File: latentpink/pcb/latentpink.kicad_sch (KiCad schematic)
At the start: 28 parts, among them M10 WEEE, M3 SCREWHOLE, M4 SCREWHOLE, M5 SCREWHOLE, M6 SCREWHOLE, M7 LONGTHING, M8 OSHW, M9 POLARITY, U36 AT30TS74_UDFN, U37 AT30TS74_UDFN, U38 AT30TS74_UDFN, U39 AT30TS74_UDFN

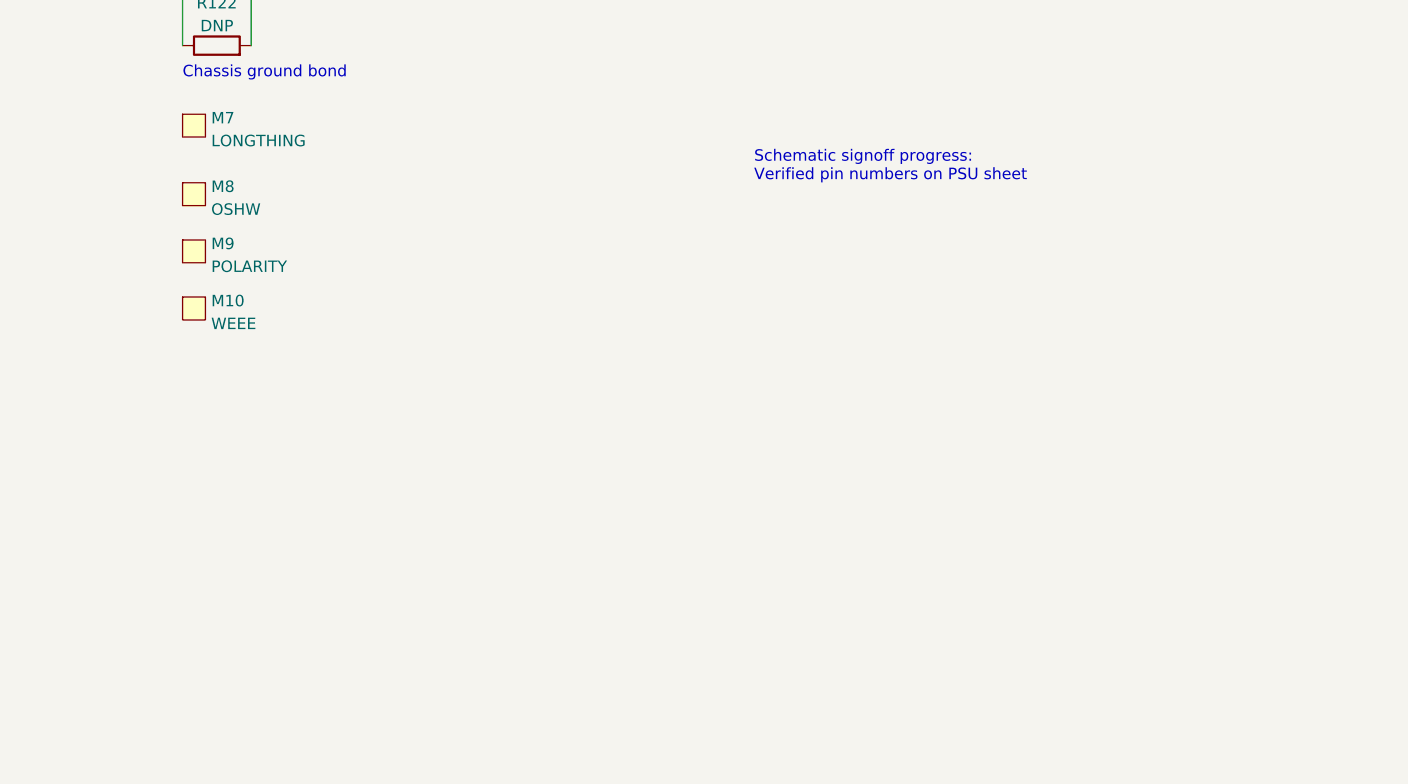
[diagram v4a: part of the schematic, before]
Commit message: Continued work on signoff review, added some more test points and SFP+ activity LEDs
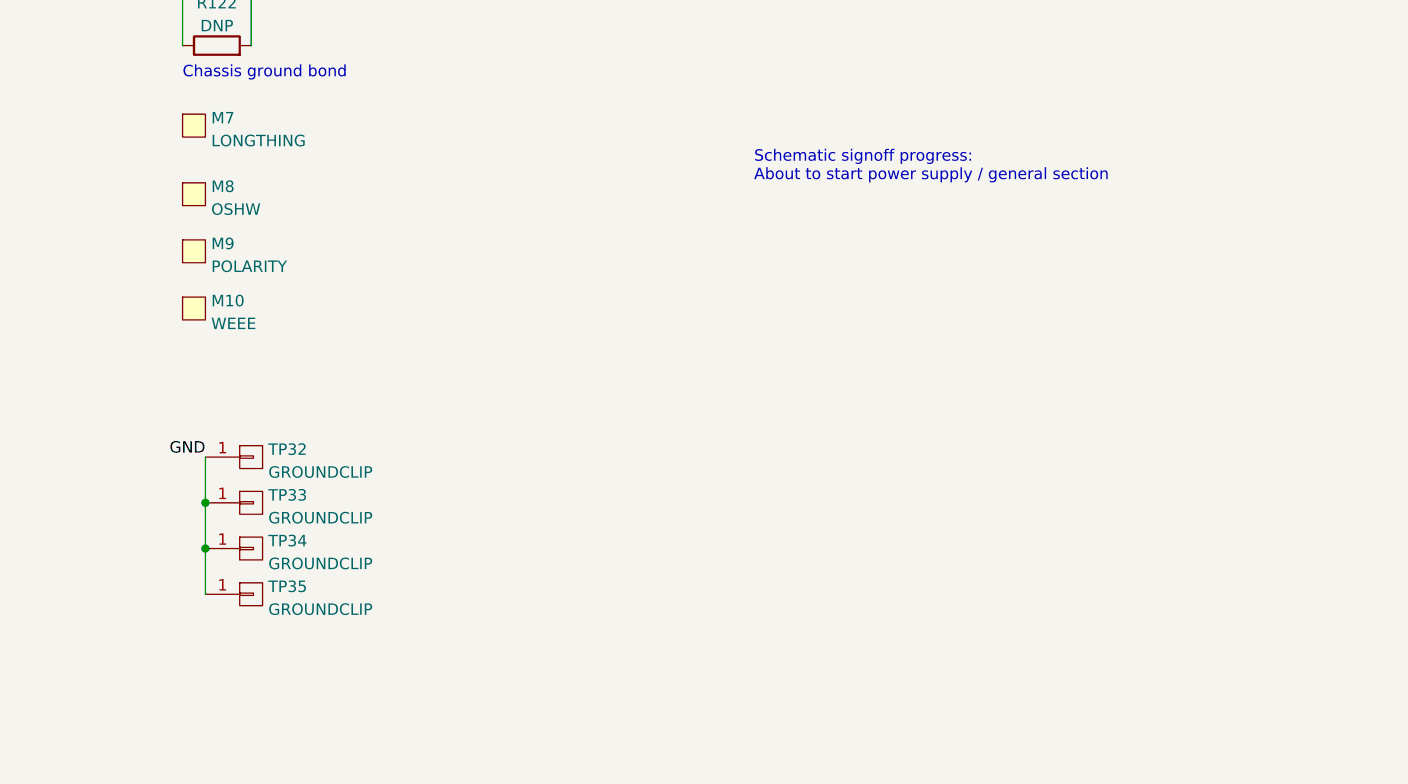
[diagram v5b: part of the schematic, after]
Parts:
- added TP32, TP33, TP34, TP35: GROUNDCLIP, azonenberg_pcb:TESTPOINT_SMT_KEYSTONE_5016, symbol conn:CONN_01X01
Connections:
- net GND: now also TP32.1 (P1), TP33.1 (P1), TP34.1 (P1), TP35.1 (P1)
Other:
- note added: "Schematic signoff progress: About to start power supply / general section"
- note removed: "Schematic signoff progress: Verified pin numbers on PSU sheet"
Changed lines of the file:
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@@
   (title_block
     (title "LATENTPINK - Top Level")
-    (date "2023-05-20")
+    (date "2023-05-21")
     (rev "0.1")
     (company "Antikernel Labs")
     (comment 1 "Andrew D. Zonenberg")
   )
+  (junction (at 72.39 173.99) (diameter 0) (color 0 0 0 0)
+  )
+  (junction (at 72.39 168.91) (diameter 0) (color 0 0 0 0)
+  )
   (no_connect (at 316.23 93.98))
   (no_connect (at 316.23 33.02))
@@
     (stroke (width 0) (type default) (color 0 0 0 0))
   )
+  (wire (pts (xy 72.39 173.99) (xy 72.39 179.07))
+    (stroke (width 0) (type default) (color 0 0 0 0))
+  )
   (wire (pts (xy 30.48 190.5) (xy 34.29 190.5))
     (stroke (width 0) (type default) (color 0 0 0 0))
@@
     (stroke (width 0) (type default) (color 0 0 0 0))
   )
+  (wire (pts (xy 72.39 168.91) (xy 72.39 173.99))
+    (stroke (width 0) (type default) (color 0 0 0 0))
+  )
   (wire (pts (xy 30.48 120.65) (xy 34.29 120.65))
     (stroke (width 0) (type default) (color 0 0 0 0))
@@
     (stroke (width 0) (type default) (color 0 0 0 0))
   )
-  (text "Schematic signoff progress:\nVerified pin numbers on PSU sheet"
+  (wire (pts (xy 72.39 163.83) (xy 72.39 168.91))
+    (stroke (width 0) (type default) (color 0 0 0 0))
+  )
+  (text "Schematic signoff progress:\nAbout to start power supply / general section"
     (at 133.35 133.35 0)
     (effects (font (size 1.27 1.27)) (justify left bottom))
@@
     (effects (font (size 1.27 1.27)) (justify left bottom))
   )
+  (label "GND" (at 72.39 163.83 180)
+    (effects (font (size 1.27 1.27)) (justify right bottom))
+  )
   (label "TEMP_I2C_SDA" (at 295.91 30.48 180)
     (effects (font (size 1.27 1.27)) (justify right bottom))
@@
     )
   )
+  (symbol (lib_id "conn:CONN_01X01") (at 77.47 168.91 0) (unit 1)
+    (in_bom yes) (on_board yes) (fields_autoplaced)
+    (property "Reference" "TP33" (id 0) (at 79.375 168.0753 0)
+      (effects (font (size 1.27 1.27)) (justify left))
+    )
+    (property "Value" "GROUNDCLIP" (id 1) (at 79.375 170.6122 0)
+      (effects (font (size 1.27 1.27)) (justify left))
+    )
+    (property "Footprint" "azonenberg_pcb:TESTPOINT_SMT_KEYSTONE_5016" (id 2) (at 77.47 168.91 0)
+      (effects (font (size 1.27 1.27)) hide)
+    )
+    (property "Datasheet" "" (id 3) (at 77.47 168.91 0)
+      (effects (font (size 1.27 1.27)) hide)
+    )
+    (pin "1")
+  )
   (symbol (lib_id "device:C") (at 337.82 44.45 0) (unit 1)
     (in_bom yes) (on_board yes) (fields_autoplaced)
@@
     (pin "2")
   )
+  (symbol (lib_id "conn:CONN_01X01") (at 77.47 173.99 0) (unit 1)
+    (in_bom yes) (on_board yes) (fields_autoplaced)
+    (property "Reference" "TP34" (id 0) (at 79.375 173.1553 0)
+      (effects (font (size 1.27 1.27)) (justify left))
+    )
+    (property "Value" "GROUNDCLIP" (id 1) (at 79.375 175.6922 0)
+      (effects (font (size 1.27 1.27)) (justify left))
+    )
+    (property "Footprint" "azonenberg_pcb:TESTPOINT_SMT_KEYSTONE_5016" (id 2) (at 77.47 173.99 0)
+      (effects (font (size 1.27 1.27)) hide)
+    )
+    (property "Datasheet" "" (id 3) (at 77.47 173.99 0)
+      (effects (font (size 1.27 1.27)) hide)
+    )
+    (pin "1")
+  )
+  (symbol (lib_id "conn:CONN_01X01") (at 77.47 163.83 0) (unit 1)
+    (in_bom yes) (on_board yes) (fields_autoplaced)
+    (property "Reference" "TP32" (id 0) (at 79.375 162.9953 0)
+      (effects (font (size 1.27 1.27)) (justify left))
+    )
+    (property "Value" "GROUNDCLIP" (id 1) (at 79.375 165.5322 0)
+      (effects (font (size 1.27 1.27)) (justify left))
+    )
+    (property "Footprint" "azonenberg_pcb:TESTPOINT_SMT_KEYSTONE_5016" (id 2) (at 77.47 163.83 0)
+      (effects (font (size 1.27 1.27)) hide)
+    )
+    (property "Datasheet" "" (id 3) (at 77.47 163.83 0)
+      (effects (font (size 1.27 1.27)) hide)
+    )
+    (pin "1")
+  )
   (symbol (lib_id "device:Ferrite_Bead_Small") (at 72.39 109.22 90) (unit 1)
     (in_bom yes) (on_board yes) (fields_autoplaced)
@@
     (pin "2")
   )
+  (symbol (lib_id "conn:CONN_01X01") (at 77.47 179.07 0) (unit 1)
+    (in_bom yes) (on_board yes) (fields_autoplaced)
+    (property "Reference" "TP35" (id 0) (at 79.375 178.2353 0)
+      (effects (font (size 1.27 1.27)) (justify left))
+    )
+    (property "Value" "GROUNDCLIP" (id 1) (at 79.375 180.7722 0)
+      (effects (font (size 1.27 1.27)) (justify left))
+    )
+    (property "Footprint" "azonenberg_pcb:TESTPOINT_SMT_KEYSTONE_5016" (id 2) (at 77.47 179.07 0)
+      (effects (font (size 1.27 1.27)) hide)
+    )
+    (property "Datasheet" "" (id 3) (at 77.47 179.07 0)
+      (effects (font (size 1.27 1.27)) hide)
+    )
+    (pin "1")
+  )
   (symbol (lib_id "conn:CONN_COAXIAL") (at 34.29 185.42 0) (unit 1)
     (in_bom yes) (on_board yes) (fields_autoplaced)
@@
       (reference "D15") (unit 1) (value "GREEN") (footprint "azonenberg_pcb:EIA_0603_LED")
     )
+    (path "/035a8a96-1dae-486c-a84e-a11c0c87b4ac/9e161449-e137-4951-be09-6af8631656a8"
+      (reference "D16") (unit 1) (value "GREEN") (footprint "azonenberg_pcb:EIA_0603_LED")
+    )
+    (path "/035a8a96-1dae-486c-a84e-a11c0c87b4ac/40a9ff30-f90c-4171-be6b-c57887c62da3"
+      (reference "D17") (unit 1) (value "GREEN") (footprint "azonenberg_pcb:EIA_0603_LED")
+    )
     (path "/70fb61fd-2f76-4850-9d6b-7e1d9a86570a/d67410e9-b9d7-4681-a748-c3dfbad70b7a"
       (reference "F1") (unit 1) (value "ERB-RD4R00X") (footprint "azonenberg_pcb:EIA_0402_CAP_NOSILK")
@@
       (reference "R163") (unit 1) (value "470") (footprint "azonenberg_pcb:EIA_0402_RES_NOSILK")
     )
+    (path "/035a8a96-1dae-486c-a84e-a11c0c87b4ac/abe3af9d-8d07-4694-83b0-02bd2d2b72e0"
+      (reference "R164") (unit 1) (value "470") (footprint "azonenberg_pcb:EIA_0402_RES_NOSILK")
+    )
+    (path "/035a8a96-1dae-486c-a84e-a11c0c87b4ac/1c30b4cc-1c78-4d4a-b045-9913b60da471"
+      (reference "R165") (unit 1) (value "470") (footprint "azonenberg_pcb:EIA_0402_RES_NOSILK")
+    )
+    (path "/70fb61fd-2f76-4850-9d6b-7e1d9a86570a/257db866-fb51-4837-970d-eba7d6636664"
+      (reference "R166") (unit 1) (value "0") (footprint "azonenberg_pcb:EIA_0402_RES_NOSILK")
+    )
     (path "/6c4b0638-d970-4292-bc58-db2e1b793524/d5990d76-6ad3-4bfd-a9be-5da547fd1224/4d701df3-1531-4e26-be52-80b3fa172f57"
       (reference "RN1") (unit 1) (value "YC124-FR-0749R9L") (footprint "azonenberg_pcb:YAGEO_YC124-FR")
@@
       (reference "TP27") (unit 1) (value "U.FL") (footprint "azonenberg_pcb:CONN_U.FL_TE_1909763-1")
     )
+    (path "/035a8a96-1dae-486c-a84e-a11c0c87b4ac/fa0e385b-60d1-42e6-bcf0-636dccf98cda"
+      (reference "TP28") (unit 1) (value "U.FL") (footprint "azonenberg_pcb:CONN_U.FL_TE_1909763-1")
+    )
+    (path "/035a8a96-1dae-486c-a84e-a11c0c87b4ac/626b4a48-b66a-4c2b-9c82-5662baf5dfe0/b911ed54-c427-4b1d-91db-cd1392145069"
+      (reference "TP29") (unit 1) (value "U.FL") (footprint "azonenberg_pcb:CONN_U.FL_TE_1909763-1")
+    )
+    (path "/035a8a96-1dae-486c-a84e-a11c0c87b4ac/626b4a48-b66a-4c2b-9c82-5662baf5dfe0/924adf40-2733-4801-9974-0af2bf57d054"
+      (reference "TP30") (unit 1) (value "U.FL") (footprint "azonenberg_pcb:CONN_U.FL_TE_1909763-1")
+    )
+    (path "/035a8a96-1dae-486c-a84e-a11c0c87b4ac/626b4a48-b66a-4c2b-9c82-5662baf5dfe0/379f5e66-dbd3-4fb9-af06-2265e254abd3"
+      (reference "TP31") (unit 1) (value "U.FL") (footprint "azonenberg_pcb:CONN_U.FL_TE_1909763-1")
+    )
+    (path "/80002df1-210f-44c9-ac86-b601402bcf9a"
+      (reference "TP32") (unit 1) (value "GROUNDCLIP") (footprint "azonenberg_pcb:TESTPOINT_SMT_KEYSTONE_5016")
+    )
+    (path "/6cab3199-1be4-40c2-a283-04f3dab278d0"
+      (reference "TP33") (unit 1) (value "GROUNDCLIP") (footprint "azonenberg_pcb:TESTPOINT_SMT_KEYSTONE_5016")
+    )
+    (path "/7d8e4008-466c-4ed6-9e0f-22ac85840f13"
+      (reference "TP34") (unit 1) (value "GROUNDCLIP") (footprint "azonenberg_pcb:TESTPOINT_SMT_KEYSTONE_5016")
+    )
+    (path "/a82424d9-c21c-40f6-88db-6f984e53482e"
+      (reference "TP35") (unit 1) (value "GROUNDCLIP") (footprint "azonenberg_pcb:TESTPOINT_SMT_KEYSTONE_5016")
+    )
     (path "/d0e7363b-23d9-4272-a4d1-0db2834b87f3/f95d26ce-f739-4ae3-935e-eb3c6ddcaea7"
